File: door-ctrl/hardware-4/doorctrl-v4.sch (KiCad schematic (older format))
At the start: 11 parts, among them CON1 ISP, CON10 5x2 header, CON2 JTAG, CON9 FTDI-serial, IC1 ATMEGA324P-A, U8 24LC64, X1 20MHz

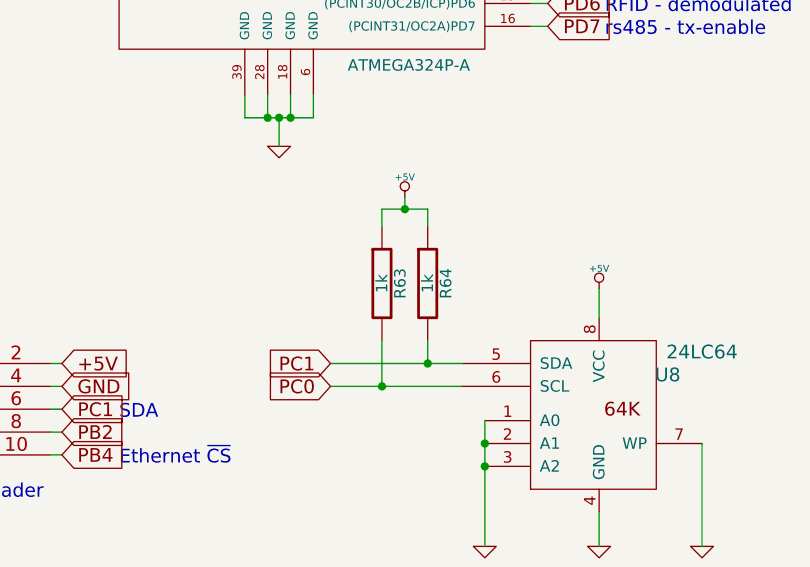
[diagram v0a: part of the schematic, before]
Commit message: Did various cleanups, added mounting holes to the schematic, so they don't disappear and grounded them, removed the redundant levelshifter
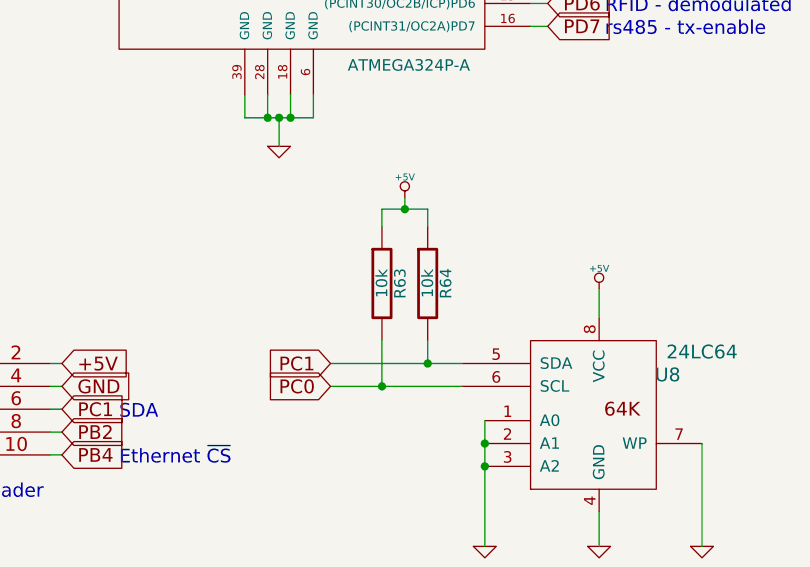
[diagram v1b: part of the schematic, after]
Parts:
- R63, R64: value 1k -> 10k
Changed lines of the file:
@@
-EESchema Schematic File Version 2  date 2011-03-10T21:41:37 CET
+EESchema Schematic File Version 2  date 2011-03-21T20:05:08 CET
 LIBS:enc28j60
 LIBS:power
@@
 LIBS:diode
 LIBS:npnpnp
+LIBS:mounting
 LIBS:doorctrl-v4-cache
 EELAYER 25  0
@@
 Sheet 1 6
 Title ""
-Date "4 feb 2011"
+Date "21 mar 2011"
 Rev ""
 Comp ""
@@
 P 3500 5675
 F 0 "R63" V 3580 5675 50  0000 C CNN
-F 1 "1k" V 3500 5675 50  0000 C CNN
+F 1 "10k" V 3500 5675 50  0000 C CNN
 	1    3500 5675
 	1    0    0    -1
@@
 P 3700 5675
 F 0 "R64" V 3780 5675 50  0000 C CNN
-F 1 "1k" V 3700 5675 50  0000 C CNN
+F 1 "10k" V 3700 5675 50  0000 C CNN
 	1    3700 5675
 	1    0    0    -1
